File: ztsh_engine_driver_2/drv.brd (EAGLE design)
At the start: 125.7 x 80.9 mm, 56 parts, among them Q1 IRF640N, Q2 IRF640N, Q3 IRF640N, Q4 IRF640N, U1 IR2110-1PBF, U2 IR2110-1PBF

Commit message: board update
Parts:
- moved X1 119.4 mm to (157.5, 165.1)
- moved JP3 115.6 mm to (-96.5, 68.6)
- moved C9 114.1 mm to (198.1, 62.9), turned to 180 degrees
- moved JP5 109.8 mm to (196.8, 74.9)
- moved Q4 106.9 mm to (-62.2, 149.9)
- moved C11 101.9 mm to (208.3, 111.8), turned to 180 degrees
- moved R7 101.8 mm to (-58.4, 101.6)
- moved C10 100.7 mm to (161.3, 48.3)
- moved D3 98.8 mm to (-50.8, 129.5)
- moved U2 96.2 mm to (-77.5, 120.7)
- moved VCC_110 94.4 mm to (209.6, 134.6), turned to 0 degrees
- moved OK2 90.9 mm to (-76.2, 88.9)
- moved C5 88.2 mm to (171.4, 140.3)
- moved D5 86.0 mm to (162.6, 134.6)
- moved OK1 82.6 mm to (-54.6, 76.2)
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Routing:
- net AGND: track 207.4 -> 0.00 mm
- net OUT1: track 121.5 -> 0.00 mm, vias 2 -> 0
- net OUT2: track 100.0 -> 0.00 mm
- net GND: track 88.3 -> 0.00 mm
- net VCC_110: track 86.4 -> 0.00 mm
- net VCC5_2: track 76.6 -> 0.00 mm
- net N$10: track 52.1 -> 0.00 mm, vias 2 -> 0
- net VCC_12_2: track 45.4 -> 0.00 mm
- net VCC_5_1: track 42.7 -> 0.00 mm
- net N$3: track 33.0 -> 0.00 mm
- net N$7: track 28.6 -> 0.00 mm, vias 2 -> 0
- net VCC_12_1: track 28.3 -> 0.00 mm
- net N$1: track 23.5 -> 0.00 mm
- net N$5: track 21.9 -> 0.00 mm, vias 2 -> 0
- net N$17: track 21.4 -> 0.00 mm
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- removed copper zone on layer 16, net 110_1
- removed copper zone on layer 16, net AGND
- removed copper zone on layer 16, net N$2
- removed copper zone on layer 16, net OUT1
- removed copper zone on layer 16, net OUT2
- removed copper zone on layer 16, net VCC_110

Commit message: board update
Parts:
- added IC1: 74AC14N, 74xx-eu:DIL14
- moved D9 161.8 mm to (87.6, 132.1)
- moved D10 152.5 mm to (36.8, 132.1)
- moved D7 140.9 mm to (66.0, 132.1)
- moved D8 126.4 mm to (15.2, 132.1)
- moved C9 121.5 mm to (78.7, 85.7), turned to 0 degrees
- moved JP5 118.2 mm to (78.7, 78.7), turned to 0 degrees
- moved OK2 117.0 mm to (22.9, 26.7)
- moved X1 115.6 mm to (50.8, 120.7), turned to 0 degrees
- moved VCC_110 107.4 mm to (111.8, 90.2), turned to 270 degrees
- moved OK1 105.6 mm to (39.4, 27.9)
- moved U2 100.0 mm to (17.8, 90.2)
- moved Q4 99.4 mm to (35.6, 132.1)
- moved C11 97.8 mm to (110.5, 111.8)
- moved C10 94.4 mm to (78.7, 94.0)
- moved Q3 87.5 mm to (15.2, 132.1), turned to 0 degrees
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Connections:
- net GND: now also IC1.7
- net VCC5_2: now also IC1.14
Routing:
- net VCC_110: track 0.00 -> 213.4 mm
- net AGND: track 0.00 -> 181.6 mm
- net OUT1: track 0.00 -> 69.1 mm
- net OUT2: track 0.00 -> 67.3 mm
- net VCC_5_1: track 0.00 -> 29.1 mm
- net N$14: track 0.00 -> 26.0 mm
- net N$9: track 0.00 -> 24.1 mm
- net N$1: track 0.00 -> 19.1 mm
- net GND: track 0.00 -> 18.9 mm
- net N$10: track 0.00 -> 17.8 mm
- net N$4: track 0.00 -> 15.9 mm
- net N$11: track 0.00 -> 12.7 mm
- net N$5: track 0.00 -> 12.1 mm
- net N$7: track 0.00 -> 10.8 mm

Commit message: board update
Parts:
- moved C17 181.0 mm to (100.3, 135.9), turned to 270 degrees
- moved C16 143.5 mm to (49.5, 135.9), turned to 270 degrees
- moved C5 98.2 mm to (78.7, 108.0), turned to 180 degrees
- moved D5 92.2 mm to (76.2, 102.2)
- moved C3 85.9 mm to (71.8, 111.1)
- moved C7 84.3 mm to (81.3, 100.3), turned to 90 degrees
- moved JP4 80.8 mm to (78.1, 113.0), turned to 180 degrees
- moved C1 71.6 mm to (72.4, 107.3)
- moved R6 2.84 mm to (85.1, 111.8)
- moved R5 2.84 mm to (66.7, 111.1)
- moved R2 1.91 mm to (88.9, 121.3)
- moved D1 1.80 mm to (63.5, 112.4)
- moved D2 1.27 mm to (89.5, 110.5)
- moved R1 1.27 mm to (67.9, 121.3)
- turned VCC_110 to 0 degrees
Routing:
- net AGND: track 181.6 -> 233.5 mm
- net VCC_12_1: track 0.00 -> 20.5 mm
- net N$15: track 0.00 -> 18.8 mm
- net VCC_110: track 213.4 -> 207.1 mm
- net N$1: track 19.1 -> 15.2 mm
- net N$4: track 15.9 -> 13.8 mm
- net OUT2: track 67.3 -> 68.5 mm
- net N$5: track 12.1 -> 12.6 mm

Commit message: board update
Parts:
- moved D7 105.4 mm to (156.2, 77.5)
- moved C3 105.4 mm to (161.9, 56.5)
- moved D2 105.4 mm to (179.7, 55.9)
- moved D9 105.4 mm to (177.8, 77.5)
- moved C1 105.4 mm to (162.6, 52.7)
- moved C10 105.4 mm to (168.9, 39.4)
- moved C17 105.4 mm to (190.5, 81.3)
- moved C5 105.4 mm to (168.9, 53.3)
- moved C9 105.4 mm to (168.9, 31.1)
- moved D5 105.4 mm to (166.4, 47.6)
- moved JP4 105.4 mm to (168.3, 58.4)
- moved JP5 105.4 mm to (168.9, 24.1)
- moved R5 105.4 mm to (156.8, 56.5)
- moved R6 105.4 mm to (175.3, 57.1)
- moved U1 105.4 mm to (158.8, 36.8)
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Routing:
- net AGND: track 233.5 -> 78.0 mm
- net VCC_110: track 207.1 -> 80.8 mm
- net OUT2: track 68.5 -> 7.62 mm
- net OUT1: track 69.1 -> 22.9 mm
- net VCC_5_1: track 29.1 -> 0.00 mm
- net VCC_12_1: track 20.5 -> 0.00 mm
- net GND: track 18.9 -> 0.00 mm
- net N$15: track 18.8 -> 0.00 mm
- net N$10: track 17.8 -> 0.00 mm
- net N$14: track 26.0 -> 11.4 mm
- net N$11: track 12.7 -> 0.00 mm
- net N$5: track 12.6 -> 0.00 mm
- net N$7: track 10.9 -> 0.00 mm
- net N$9: track 24.1 -> 14.0 mm
- net N$1: track 15.2 -> 8.89 mm
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
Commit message: board update...
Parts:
- moved D1 139.8 mm to (17.8, 90.8)
- moved U1 139.2 mm to (24.1, 72.4)
- moved R5 138.9 mm to (22.2, 90.8)
- moved D2 135.6 mm to (48.9, 91.4)
- moved R6 135.2 mm to (44.5, 91.4)
- moved R8 117.9 mm to (103.5, 90.8)
- moved D4 117.1 mm to (108.0, 90.8)
- moved U2 113.5 mm to (85.1, 73.7)
- moved D3 113.4 mm to (77.5, 91.4)
- moved R7 112.4 mm to (82.5, 91.4)
- moved D9 102.4 mm to (83.8, 118.1)
- moved D7 96.7 mm to (67.3, 115.6)
- moved D10 94.1 mm to (86.4, 127.0)
- moved C11 86.4 mm to (154.9, 180.3)
- moved D8 83.9 mm to (40.6, 127.0)
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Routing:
- net OUT2: track 7.62 -> 104.1 mm
- net OUT1: track 22.9 -> 111.8 mm
- net VCC_110: track 80.8 -> 135.9 mm, vias 0 -> 2
- net N$7: track 0.00 -> 15.9 mm
- net AGND: track 78.0 -> 64.2 mm
- net N$11: track 0.00 -> 13.3 mm
- net N$10: track 0.00 -> 12.7 mm
- net N$5: track 0.00 -> 12.1 mm
- net N$1: track 8.89 -> 19.7 mm
- net N$4: track 10.8 -> 17.8 mm
- net N$14: track 11.4 -> 17.8 mm
- net N$9: track 14.0 -> 19.0 mm

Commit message: board update
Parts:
- Q1, Q2, Q3, Q4: device transistor-power:TO220AH -> transistor-power:TO262-V
- R11, R12: device rcl:R0805 -> rcl:0204V
- moved JP5 185.2 mm to (31.8, 148.6), turned to 180 degrees
- moved C9 171.4 mm to (31.8, 134.0), turned to 180 degrees
- moved C10 148.6 mm to (39.4, 121.9), turned to 90 degrees
- moved C7 146.6 mm to (41.9, 114.3)
- moved D5 137.0 mm to (48.9, 118.1), turned to 90 degrees
- moved C5 131.0 mm to (53.3, 114.9), turned to 270 degrees
- moved C3 128.2 mm to (52.1, 122.6), turned to 270 degrees
- moved C1 127.7 mm to (55.2, 121.9), turned to 270 degrees
- moved JP4 123.3 mm to (59.1, 115.6), turned to 270 degrees
- moved R12 118.7 mm to (35.6, 99.1), flipped to the bottom
- moved C17 113.2 mm to (78.7, 99.1)
- moved R11 107.8 mm to (34.3, 104.1), flipped to the bottom
- moved JP1 106.5 mm to (59.7, 80.0), turned to 270 degrees
- moved OK1 106.5 mm to (-15.2, 119.4), turned to 270 degrees
- moved C2 103.0 mm to (55.9, 86.4), turned to 270 degrees
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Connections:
- net AGND: now also Q2.3, Q4.3; no longer Q2.E, Q4.E
- net N$1: now also Q1.1; no longer Q1.B
- net N$14: now also Q4.1; no longer Q4.B
- net N$4: now also Q2.1; no longer Q2.B
- net N$9: now also Q3.1; no longer Q3.B
- net OUT1: now also Q3.3, Q4.2; no longer Q3.E, Q4.C
- net OUT2: now also Q1.3, Q2.2; no longer Q1.E, Q2.C
- net VCC_110: now also Q1.2, Q3.2; no longer Q1.C, Q3.C
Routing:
- net AGND: track 64.2 -> 365.1 mm, vias 0 -> 2
- net GND: track 0.00 -> 63.8 mm
- net N$16: track 0.00 -> 48.3 mm
- net OUT2: track 104.1 -> 145.8 mm
- net N$19: track 0.00 -> 35.6 mm
- net VCC_12_2: track 0.00 -> 21.1 mm
- net VCC_12_1: track 0.00 -> 20.7 mm
- net VCC_110: track 135.9 -> 155.0 mm
- net N$15: track 0.00 -> 17.5 mm
- net N$17: track 0.00 -> 12.6 mm
- net N$7: track 15.9 -> 9.73 mm
- net N$1: track 19.7 -> 16.5 mm
- net VCC_5_1: track 0.00 -> 2.86 mm
- net VCC5_2: track 0.00 -> 2.86 mm
- net N$5: track 12.1 -> 9.52 mm
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
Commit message: board update (near finish, hope...)
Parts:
- added D13, D14, D15, D16: (no value), adafruit:DO-1N4148
- added R13, R14, R15, R16: (no value), resistor:0204/7
- moved D12 168.0 mm to (-73.7, 143.5)
- moved D11 127.7 mm to (-85.1, 129.5)
- moved IC1 108.6 mm to (24.1, 102.9), turned to 90 degrees
- moved C12 102.6 mm to (38.1, 96.5)
- moved OK1 49.0 mm to (14.0, 80.0)
- moved OK2 35.6 mm to (14.0, 125.7)
- moved R11 29.3 mm to (25.4, 76.2)
- moved R12 26.2 mm to (25.4, 123.2)
- moved C9 7.01 mm to (32.4, 127.0), turned to 90 degrees
- moved C17 4.02 mm to (74.9, 100.3), turned to 0 degrees
- moved D7 1.27 mm to (85.1, 124.5)
- moved D9 1.27 mm to (85.1, 80.0)
- moved C16 1.27 mm to (99.1, 129.5)
- moved D10 1.27 mm to (92.7, 80.0)
- moved D8 1.27 mm to (92.7, 124.5)
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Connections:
- new net N$18: D14.A, IC1.9, OK2.5, R12.2
- new net N$2: D15.A, IC1.13, OK1.5, R11.2
- new net N$20: D13.C, R15.1
- new net N$21: D14.C, IC1.11, R13.2, R15.2
- new net N$22: D13.A, IC1.12, R13.1
- new net N$23: D16.C, R14.1
- new net N$24: D15.C, IC1.1, R14.2, R16.2
- new net N$25: D16.A, IC1.8, R16.1
- net N$16: now also IC1.10; no longer OK1.5, R11.2
- net N$19: now also IC1.2; no longer OK2.5, R12.2
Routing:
- net GND: track 63.8 -> 116.1 mm
- net OUT2: track 145.8 -> 99.7 mm
- net VCC5_2: track 2.86 -> 47.6 mm, vias 0 -> 2
- net N$2: track 0.00 -> 38.1 mm
- net N$18: track 0.00 -> 34.3 mm
- net AGND: track 365.1 -> 331.6 mm
- net N$21: track 0.00 -> 31.8 mm
- net N$24: track 0.00 -> 30.5 mm
- net N$16: track 48.3 -> 69.8 mm
- net N$22: track 0.00 -> 10.2 mm
- net N$19: track 35.6 -> 43.2 mm
- net VCC_5_1: track 2.86 -> 10.1 mm
- net N$25: track 0.00 -> 6.35 mm
- net N$15: track 17.5 -> 11.4 mm
- net VCC_110: track 155.0 -> 149.5 mm
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
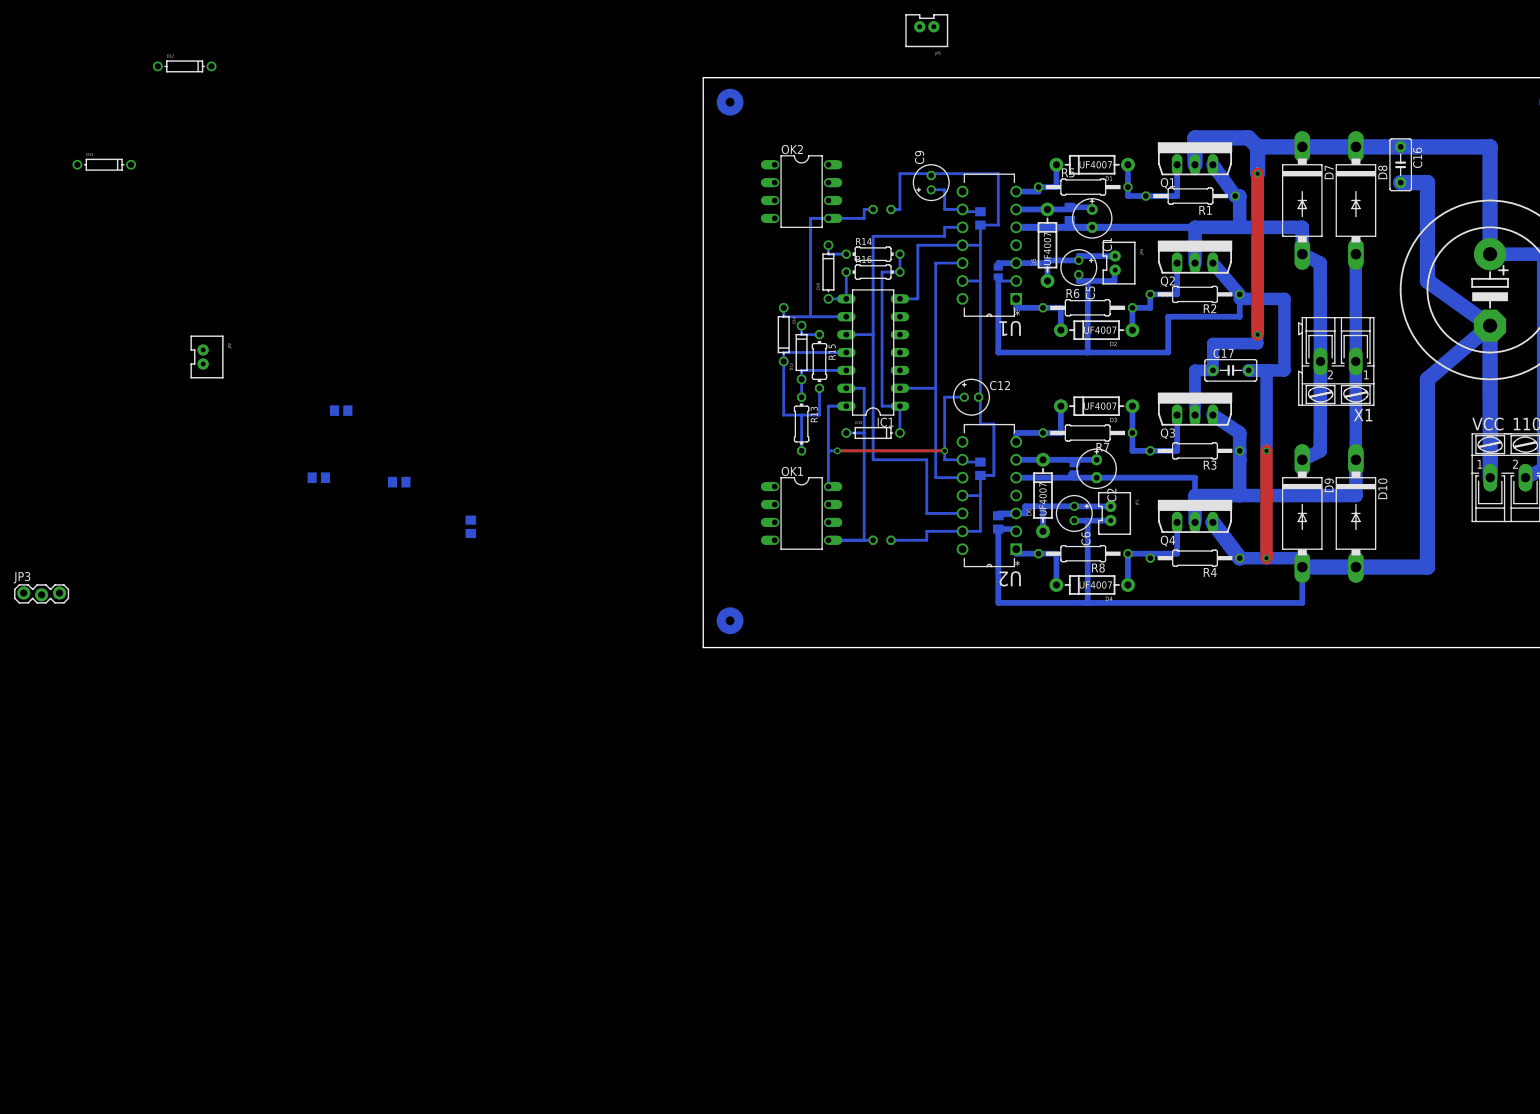
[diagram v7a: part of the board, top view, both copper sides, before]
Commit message: schematic update using 74hc00
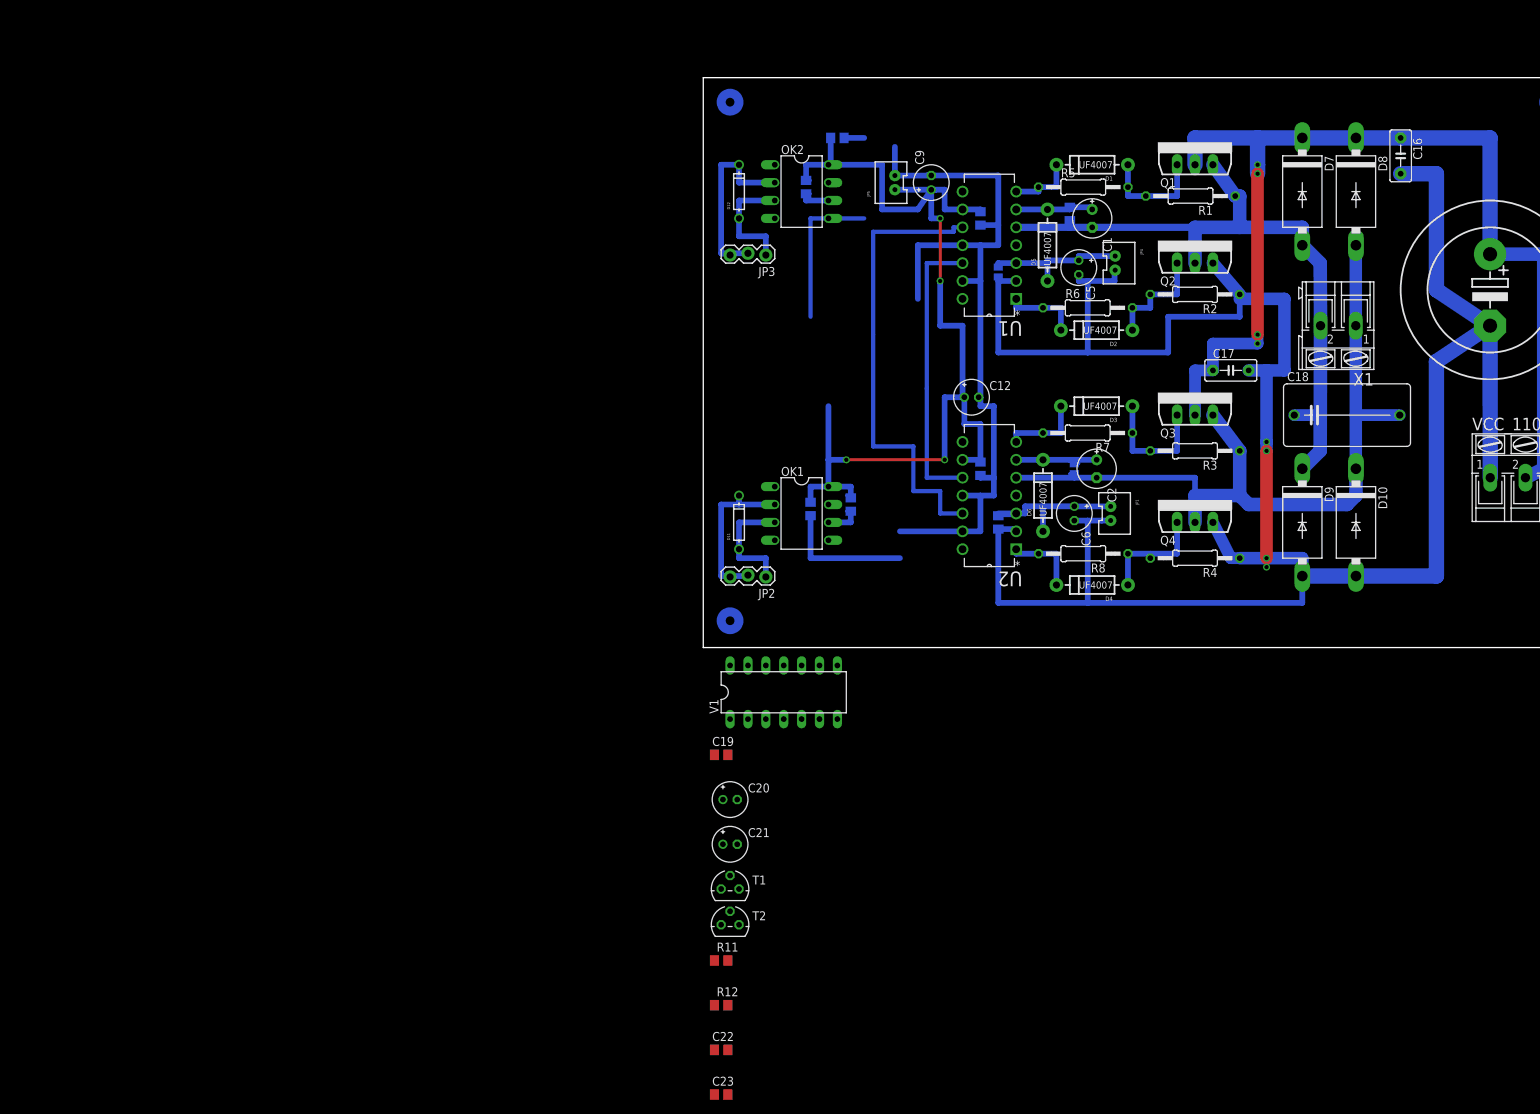
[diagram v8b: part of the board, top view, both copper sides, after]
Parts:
- removed D13, D14, D15, D16: (no value), adafruit:DO-1N4148
- removed IC1: 74AC14N, 74xx-eu:DIL14
- removed R13, R14, R15, R16: (no value), resistor:0204/7
- added C18: (no value), resistor:C150-091X182
- added C19, C22, C23: 100nF, rcl:C0805
- added C20, C21: 10µF, rcl:E2-5
- added T1, T2: BC547, transistor:TO92
- added V1: 74HC00N, 74ttl-din:DIL14
- JP2: value 5v -> (none); device SparkFun-Connectors:JST-2-PTH-VERT -> SparkFun-Connectors:1X03_LOCK
- R10, R9: value (none) -> 570
- R11, R12: value (none) -> 570; device rcl:0204V -> rcl:R0805
- moved JP3 115.9 mm to (8.89, 116.8), turned to 180 degrees
- moved R12 115.3 mm to (2.54, 10.2), flipped to the top
- moved D11 103.5 mm to (5.08, 78.7), turned to 90 degrees
- moved C14 88.1 mm to (19.1, 133.3)
- moved JP2 85.3 mm to (8.89, 71.1), turned to 180 degrees
- moved D12 80.7 mm to (5.08, 125.7), turned to 90 degrees
- moved R10 73.3 mm to (14.6, 126.4), turned to 90 degrees
- moved R9 64.2 mm to (21.0, 81.3), turned to 90 degrees
- moved R11 63.9 mm to (2.54, 16.5), flipped to the top
- moved C15 48.3 mm to (15.2, 80.6)
- moved JP5 22.2 mm to (26.7, 127.0), turned to 90 degrees
- moved X1 5.08 mm to (90.2, 106.7)
- moved C16 1.27 mm to (99.1, 130.8)
- moved D10 1.27 mm to (92.7, 78.7)
- moved D7 1.27 mm to (85.1, 125.7)
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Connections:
- removed net N$21: D14.C, IC1.11, R13.2, R15.2
- removed net N$25: D16.A, IC1.8, R16.1
- removed net VCC5_2: C12.+, C13.1, C14.1, C15.1, IC1.14, JP2.1, OK1.8, OK2.8, R10.2, R9.2, U2.9
- removed net VCC_5_1: C10.2, C9.+, JP5.1, U1.9
- new net N$26: D12.C, JP3.2, JP3.3, OK2.2
- new net VCC: C10.2, C12.+, C13.1, C14.1, C15.1, C19.1, C20.+, C21.+, C9.+, JP5.1, OK1.8, OK2.8, R10.2, R9.2, U1.9, U2.9, V1.14
- net GND: now also C19.2, C20.-, C21.-, C22.2, C23.2, T1.1, T2.1, V1.7; no longer IC1.7, JP2.2, R11.1, R12.1
- net N$13: now also V1.1, V1.2, V1.4, V1.5
- net N$16: now also T1.3, V1.3; no longer IC1.10
- net N$18: no longer D14.A, IC1.9, R12.2
- net N$19: now also T2.3, V1.8; no longer IC1.2
- net N$2: no longer D15.A, IC1.13, R11.2
- net N$20: now also R11.2, V1.11; no longer D13.C, R15.1
- net N$22: now also C22.1, R11.1, T1.2; no longer D13.A, IC1.12, R13.1
- net N$23: now also C23.1, R12.1, T2.2; no longer D16.C, R14.1
- net N$24: now also R12.2, V1.6; no longer D15.C, IC1.1, R14.2, R16.2
- net N$3: now also JP2.2, JP2.3; no longer D12.C, JP3.3, OK2.2
- net N$6: now also JP2.1; no longer JP3.2
- net N$8: now also V1.10, V1.12, V1.13, V1.9
- net OUT1: now also C18.2
- net OUT2: now also C18.1
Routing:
- net VCC: track 0.00 -> 147.7 mm, vias 0 -> 4
- net VCC5_2: track 47.6 -> 0.00 mm, vias 2 -> 0
- net N$2: track 38.1 -> 0.00 mm
- net N$21: track 31.8 -> 0.00 mm
- net N$24: track 30.5 -> 0.00 mm
- net N$26: track 0.00 -> 28.1 mm
- net N$3: track 0.00 -> 23.2 mm
- net GND: track 116.1 -> 136.2 mm
- net N$6: track 0.00 -> 16.6 mm
- net N$12: track 0.00 -> 16.6 mm
- net N$18: track 34.3 -> 21.6 mm
- net N$22: track 10.2 -> 0.00 mm
- net VCC_5_1: track 10.1 -> 0.00 mm
- net OUT1: track 108.6 -> 116.4 mm
- net N$25: track 6.35 -> 0.00 mm
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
